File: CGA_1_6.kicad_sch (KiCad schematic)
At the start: 19 parts, among them U13 74LS08, U14 74S32, U28 74S10, U38 MC6845, U48 74LS51, U49 74LS02, U50 2118, U51 2118, U52 2118, U53 2118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

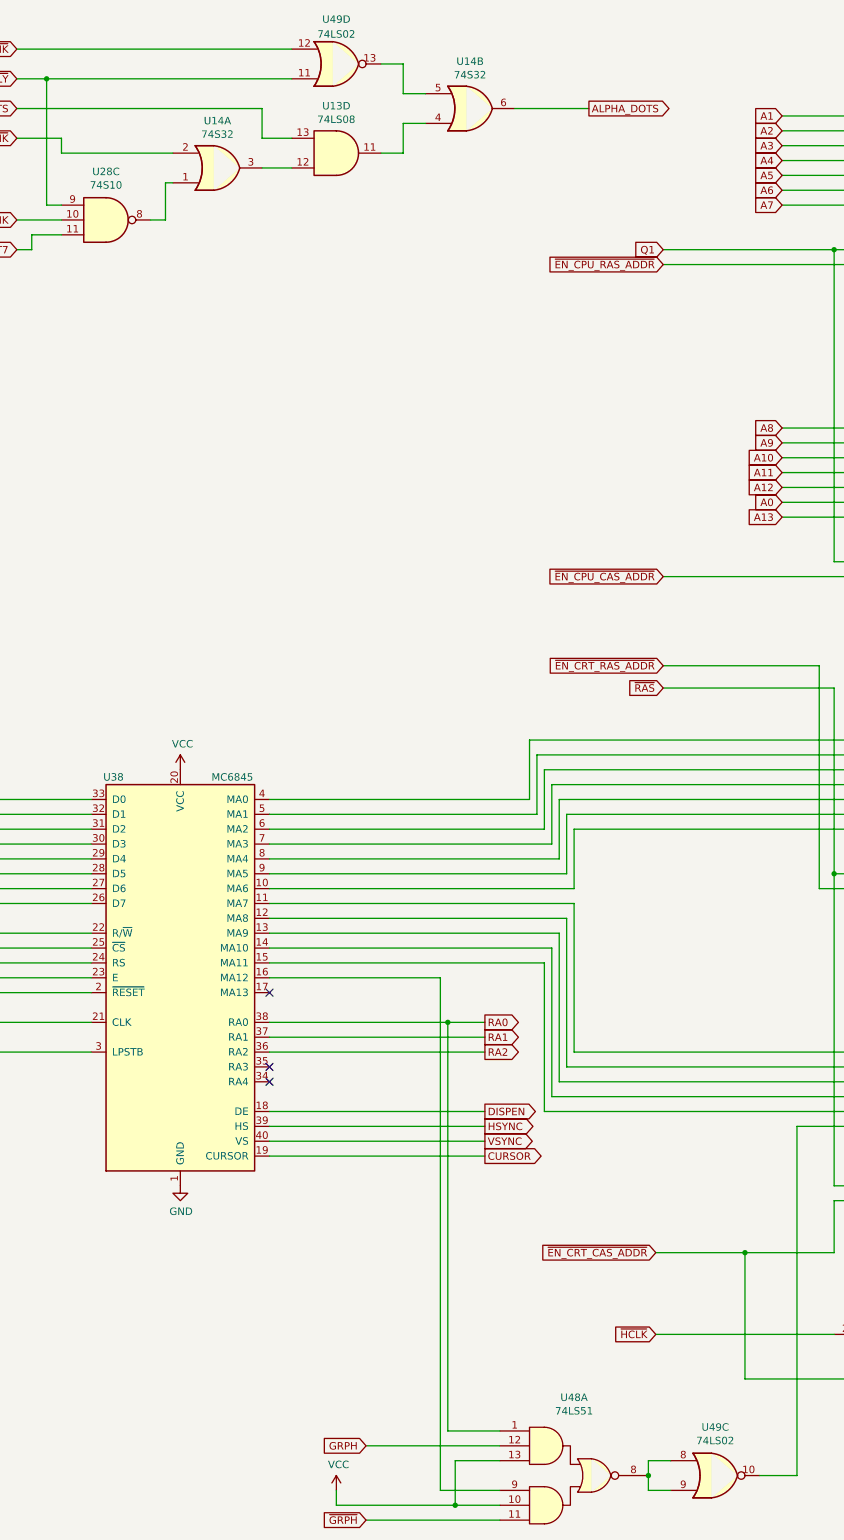
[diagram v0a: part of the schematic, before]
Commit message: Fix Q1' naming thanks to Michael Karcher
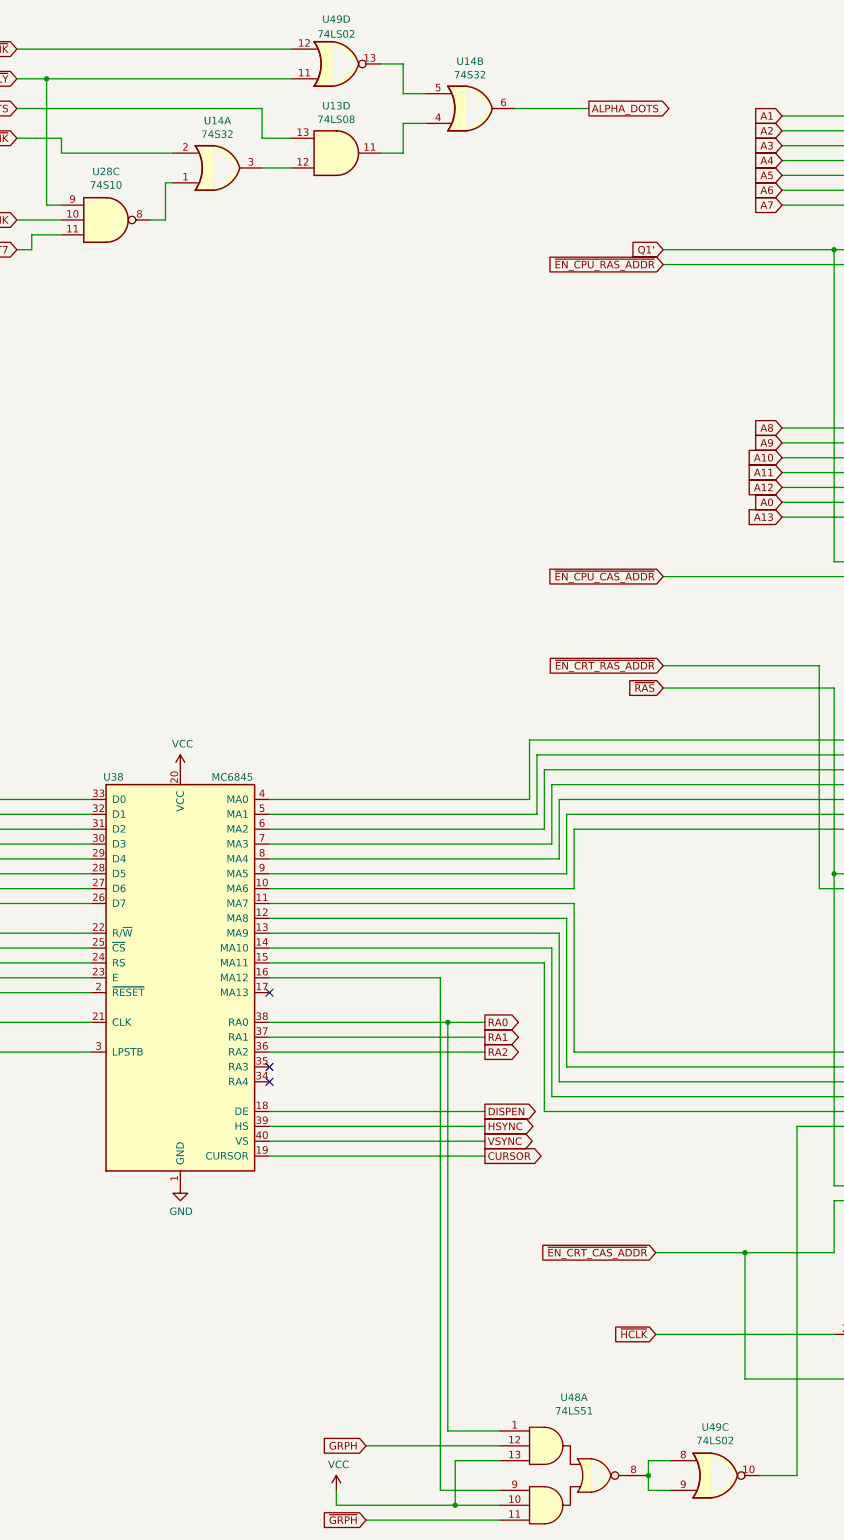
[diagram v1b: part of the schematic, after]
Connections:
- net Q1 renamed Q1'
